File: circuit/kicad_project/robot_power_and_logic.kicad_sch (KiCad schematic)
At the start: 17 parts, among them J1 HC-05 connection socket, M1 Motor_DC, M2 Motor_DC, SW1 SW_SPST, SW2 SW_SPST, U1 LM7805_TO220, U2 Pico, U3 L293D, U4 L293D

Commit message: Assign capacitor footprints
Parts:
- C1, C2, C3, C4, C5, C6: footprint (none) -> Capacitor_THT:C_Disc_D4.7mm_W2.5mm_P5.00mm
- J1: footprint (none) -> Connector_PinHeader_2.54mm:PinHeader_1x04_P2.54mm_Vertical
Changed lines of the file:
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@@
       (effects (font (size 1.27 1.27)) (justify right))
     )
-    (property "Footprint" "" (id 2) (at 60.6552 53.34 0)
+    (property "Footprint" "Capacitor_THT:C_Disc_D4.7mm_W2.5mm_P5.00mm" (id 2) (at 60.6552 53.34 0)
       (effects (font (size 1.27 1.27)) hide)
     )
@@
       (effects (font (size 1.27 1.27)) (justify left))
     )
-    (property "Footprint" "" (id 2) (at 273.3548 40.64 0)
+    (property "Footprint" "Capacitor_THT:C_Disc_D4.7mm_W2.5mm_P5.00mm" (id 2) (at 273.3548 40.64 0)
       (effects (font (size 1.27 1.27)) hide)
     )
@@
       (effects (font (size 1.27 1.27)) (justify left))
     )
-    (property "Footprint" "" (id 2) (at 326.6948 44.45 0)
+    (property "Footprint" "Capacitor_THT:C_Disc_D4.7mm_W2.5mm_P5.00mm" (id 2) (at 326.6948 44.45 0)
       (effects (font (size 1.27 1.27)) hide)
     )
@@
       (effects (font (size 1.27 1.27)) (justify left))
     )
-    (property "Footprint" "" (id 2) (at 118.11 26.67 0)
+    (property "Footprint" "Connector_PinHeader_2.54mm:PinHeader_1x04_P2.54mm_Vertical" (id 2) (at 118.11 26.67 0)
       (effects (font (size 1.27 1.27)) hide)
     )
@@
       (effects (font (size 1.27 1.27)) (justify left))
     )
-    (property "Footprint" "" (id 2) (at 79.7052 53.34 0)
+    (property "Footprint" "Capacitor_THT:C_Disc_D4.7mm_W2.5mm_P5.00mm" (id 2) (at 79.7052 53.34 0)
       (effects (font (size 1.27 1.27)) hide)
     )
@@
       (effects (font (size 1.27 1.27)) (justify left))
     )
-    (property "Footprint" "" (id 2) (at 239.0648 43.18 0)
+    (property "Footprint" "Capacitor_THT:C_Disc_D4.7mm_W2.5mm_P5.00mm" (id 2) (at 239.0648 43.18 0)
       (effects (font (size 1.27 1.27)) hide)
     )
@@
       (effects (font (size 1.27 1.27)) (justify left))
     )
-    (property "Footprint" "" (id 2) (at 202.2348 43.18 0)
+    (property "Footprint" "Capacitor_THT:C_Disc_D4.7mm_W2.5mm_P5.00mm" (id 2) (at 202.2348 43.18 0)
       (effects (font (size 1.27 1.27)) hide)
     )
@@
     )
     (path "/61d6f7e6-a87d-446b-b175-878eaf1c21b6"
-      (reference "C1") (unit 1) (value "330 nF") (footprint "")
+      (reference "C1") (unit 1) (value "330 nF") (footprint "Capacitor_THT:C_Disc_D4.7mm_W2.5mm_P5.00mm")
     )
     (path "/c2903e07-597a-4301-9223-2a40880240f0"
-      (reference "C2") (unit 1) (value "100 nF") (footprint "")
+      (reference "C2") (unit 1) (value "100 nF") (footprint "Capacitor_THT:C_Disc_D4.7mm_W2.5mm_P5.00mm")
     )
     (path "/fca2c83d-9830-4e32-959c-68f0e150a796"
-      (reference "C3") (unit 1) (value "100 nF") (footprint "")
+      (reference "C3") (unit 1) (value "100 nF") (footprint "Capacitor_THT:C_Disc_D4.7mm_W2.5mm_P5.00mm")
     )
     (path "/f101e1c0-211d-4a8f-9d4c-05b816db0f43"
-      (reference "C4") (unit 1) (value "1 µF") (footprint "")
+      (reference "C4") (unit 1) (value "1 µF") (footprint "Capacitor_THT:C_Disc_D4.7mm_W2.5mm_P5.00mm")
     )
     (path "/6798faec-2cd2-4173-851a-04878eeaa12f"
-      (reference "C5") (unit 1) (value "100 nF") (footprint "")
+      (reference "C5") (unit 1) (value "100 nF") (footprint "Capacitor_THT:C_Disc_D4.7mm_W2.5mm_P5.00mm")
     )
     (path "/a7f62dd3-dac8-4de4-b3c8-608044099ec8"
-      (reference "C6") (unit 1) (value "1 µF") (footprint "")
+      (reference "C6") (unit 1) (value "1 µF") (footprint "Capacitor_THT:C_Disc_D4.7mm_W2.5mm_P5.00mm")
     )
     (path "/bbb45523-5adb-447f-acec-3bd3a8e2044a"
-      (reference "J1") (unit 1) (value "HC-05 connection socket") (footprint "")
+      (reference "J1") (unit 1) (value "HC-05 connection socket") (footprint "Connector_PinHeader_2.54mm:PinHeader_1x04_P2.54mm_Vertical")
     )
     (path "/a1814adc-4ac2-4263-9209-7cd9c36fb2df"

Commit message: Add title, date and revision number
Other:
- title: (none) -> Robot power and logic
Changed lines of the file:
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@@
 (kicad_sch (version 20211123) (generator eeschema)
   (paper "A3")
+  (title_block
+    (title "Robot power and logic")
+    (date "2023-02-07")
+    (rev "1")
+  )
   (junction (at 203.2 43.18) (diameter 0) (color 0 0 0 0)
   )

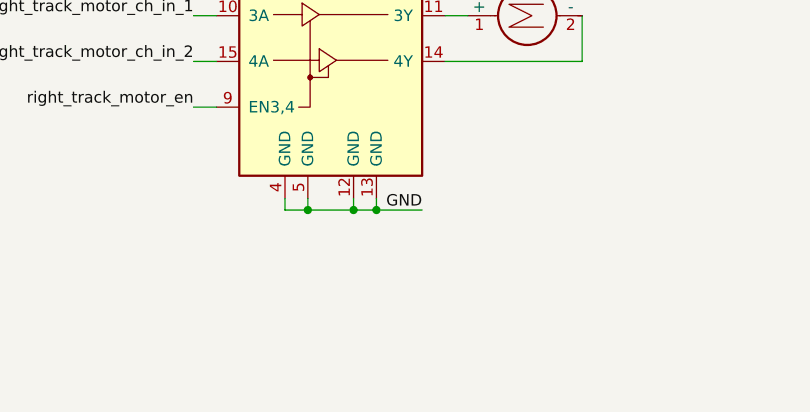
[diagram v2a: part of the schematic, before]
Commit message: Add L293D soldering info
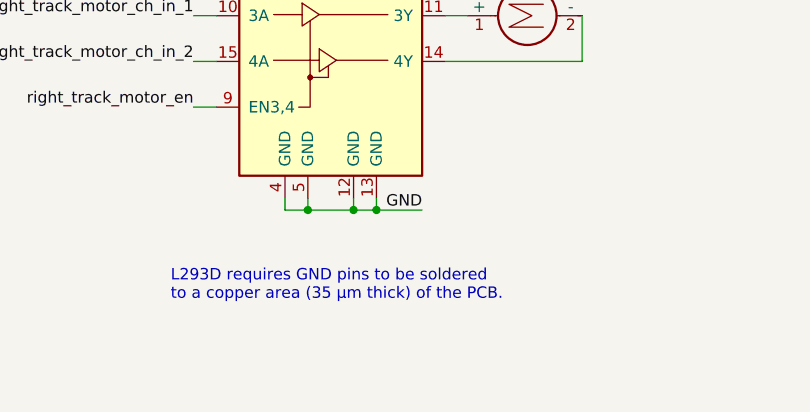
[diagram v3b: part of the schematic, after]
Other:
- note added: "L293D requires GND pins to be soldered to a copper area (35 µm thick) of the PCB."

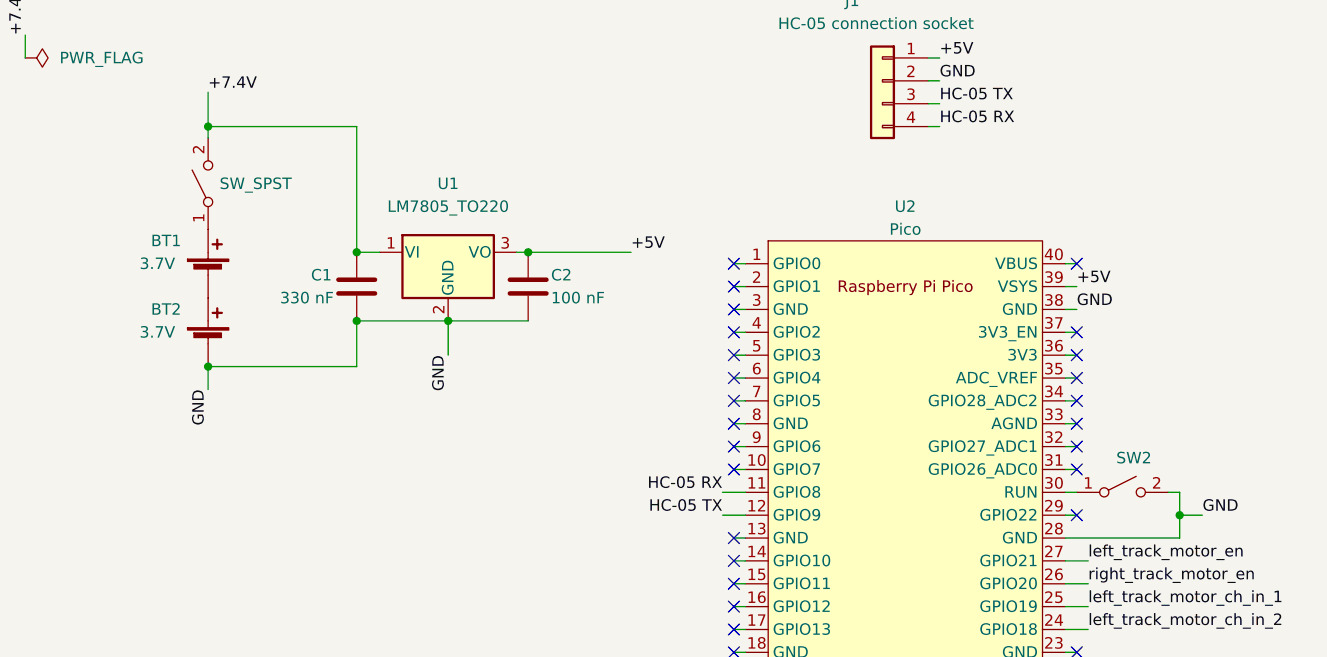
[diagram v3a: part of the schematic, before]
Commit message: Replace spst reset switch with push button switch
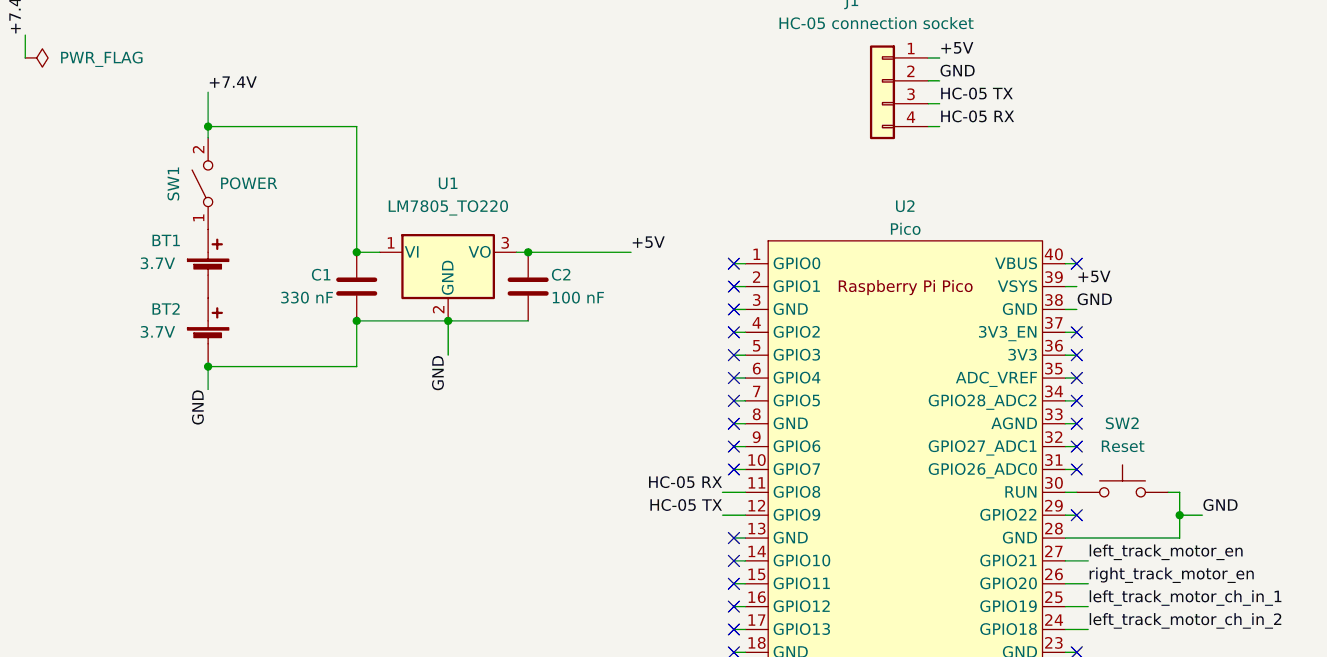
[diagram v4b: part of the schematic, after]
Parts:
- removed SW2: SW_SPST, Button_Switch_THT:SW_PUSH_6mm_H4.3mm, symbol Switch:SW_SPST
- added SW2: Reset, symbol Switch:SW_Push
- SW1: value SW_SPST -> POWER
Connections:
- net GND: now also SW2.2
- net at U2.30 (RUN): now also SW2.1
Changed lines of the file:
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@@
   )
   (symbol (lib_id "Switch:SW_SPST") (at 43.18 38.1 90) (unit 1)
-    (in_bom yes) (on_board no) (fields_autoplaced)
-    (property "Reference" "SW1" (id 0) (at 36.83 38.1 0)
-      (effects (font (size 1.27 1.27)) hide)
-    )
-    (property "Value" "SW_SPST" (id 1) (at 44.45 38.0999 90)
+    (in_bom yes) (on_board no)
+    (property "Reference" "SW1" (id 0) (at 39.37 38.1 0))
+    (property "Value" "POWER" (id 1) (at 44.45 38.0999 90)
       (effects (font (size 1.27 1.27)) (justify right))
     )
@@
     )
     (property "Datasheet" "~" (id 3) (at 274.32 44.45 0)
+      (effects (font (size 1.27 1.27)) hide)
+    )
+    (pin "1")
+    (pin "2")
+  )
+  (symbol (lib_id "Switch:SW_Push") (at 144.78 72.39 0) (unit 1)
+    (in_bom yes) (on_board yes) (fields_autoplaced)
+    (property "Reference" "SW2" (id 0) (at 144.78 64.77 0))
+    (property "Value" "Reset" (id 1) (at 144.78 67.31 0))
+    (property "Footprint" "" (id 2) (at 144.78 67.31 0)
+      (effects (font (size 1.27 1.27)) hide)
+    )
+    (property "Datasheet" "~" (id 3) (at 144.78 67.31 0)
       (effects (font (size 1.27 1.27)) hide)
     )
@@
     (pin "9")
   )
-  (symbol (lib_id "Switch:SW_SPST") (at 144.78 72.39 0) (unit 1)
-    (in_bom yes) (on_board yes)
-    (property "Reference" "SW2" (id 0) (at 146.05 68.58 0))
-    (property "Value" "SW_SPST" (id 1) (at 146.05 69.85 0)
-      (effects (font (size 1.27 1.27)) hide)
-    )
-    (property "Footprint" "Button_Switch_THT:SW_PUSH_6mm_H4.3mm" (id 2) (at 144.78 72.39 0)
-      (effects (font (size 1.27 1.27)) hide)
-    )
-    (property "Datasheet" "~" (id 3) (at 144.78 72.39 0)
-      (effects (font (size 1.27 1.27)) hide)
-    )
-    (pin "1")
-    (pin "2")
-  )
   (symbol (lib_id "Device:C") (at 240.03 46.99 180) (unit 1)
     (in_bom yes) (on_board yes)
@@
     )
     (path "/1a791175-8f72-4b31-ac4b-16064e9ebdb0"
-      (reference "SW1") (unit 1) (value "SW_SPST") (footprint "")
-    )
-    (path "/df03d3a0-9004-4ed1-8801-d288ae91ff11"
-      (reference "SW2") (unit 1) (value "SW_SPST") (footprint "Button_Switch_THT:SW_PUSH_6mm_H4.3mm")
+      (reference "SW1") (unit 1) (value "POWER") (footprint "")
+    )
+    (path "/81ade2cd-bc57-45b8-89e6-f66033347ac0"
+      (reference "SW2") (unit 1) (value "Reset") (footprint "")
     )
     (path "/87c63aec-2711-4c05-adcb-ded7e9118eaf"
